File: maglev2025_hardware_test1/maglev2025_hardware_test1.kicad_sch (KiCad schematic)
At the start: 5 parts, among them U1 STM32G474RBTx, U2 ICM-42688-P, U3 LIS3MDLTR, U4 AT8236

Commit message: update
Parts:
- added C1: 10u, Capacitor_SMD:C_1206_3216Metric, symbol Device:C
- added C2: 100u 25V, Capacitor_THT:CP_Radial_D6.3mm_P2.50mm, symbol Device:C_Polarized
- added R1: 10m, Resistor_SMD:R_2512_6332Metric, symbol Device:R_US
- added R2: 100m, Resistor_SMD:R_2512_6332Metric, symbol Device:R
- added U5: INA240A1PW, Package_SO:TSSOP-8_4.4x3mm_P0.65mm, symbol Amplifier_Current:INA240A1PW
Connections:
- net at L1.1 (-): now also U4.6 (OUT1)
- net at L1.2 (+): now also R1.1, U5.2 (+)
- net GND: now reaches U4.1 (GND), U4.9 (GND)
- net GND: now also C1.2, C2.2, R2.1, U5.1 (GND), U5.4 (GND), U5.6 (REF2)
- net CTRL_A2: now reaches U4.2 (IN2)
- net CTRL_A1: now reaches U4.3 (IN1)
- net +3.3V: now reaches U4.4 (VREF)
- net +3.3V: now also U5.5 (V+), U5.7 (REF1)
- net VPP: now reaches U4.5 (VM)
- net VPP: now also C1.1, C2.1
- net at U4.7 (ISEN): now also R2.2
- net at U4.8 (OUT2): now also R1.2, U5.3 (-)
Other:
- moved on the sheet: L1, U2, U4

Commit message: schemetic and pin assignment
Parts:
- removed U2: ICM-42688-P, 0_RM2024:PQFN50P300X250X97-14N, symbol 0_RM2024:ICM-42688-P
- removed U3: LIS3MDLTR, 0_RM2024:XDCR_LIS3MDLTR, symbol 0_RM2024:LIS3MDLTR
- added C10, C9: 100u 16V, Capacitor_THT:CP_Radial_D6.3mm_P2.50mm, symbol Device:C_Polarized
- added C11: 10u, Capacitor_SMD:C_0603_1608Metric, symbol Device:C
- added C12, C13, C14, C15, C16, C17, C18, C19, C20, C23, C25, C27, C28, C31, C32, C33: 100n, Capacitor_SMD:C_0603_1608Metric, symbol Device:C
- added C21, C30, C40, C41: 100n, Capacitor_SMD:C_0603_1608Metric, symbol Device:C_Small
- added C22: 20p, Capacitor_SMD:C_0603_1608Metric, symbol Device:C_Small
- added C24, C26, C29: 10u, Capacitor_SMD:C_1206_3216Metric, symbol Device:C_Small
- added C3, C5, C6: 10u, Capacitor_SMD:C_1206_3216Metric, symbol Device:C
- added C36, C39, C78: 10u, Capacitor_SMD:C_0603_1608Metric, symbol Device:C_Small
- added C38: 10n, Capacitor_SMD:C_0603_1608Metric, symbol Device:C_Small
- added C4, C7, C8: 100u 25V, Capacitor_THT:CP_Radial_D6.3mm_P2.50mm, symbol Device:C_Polarized
- added D4: SMAJ12A, Diode_SMD:D_SMA, symbol Diode:SMAJ24A
- added D5: SMF5.0A, Diode_SMD:D_SMF, symbol Diode:SMAJ5.0A
- added F1: 1A, Fuse:Fuse_1206_3216Metric, symbol Device:Fuse
- added J20: PWRIn, Connector_AMASS:AMASS_XT30U-M_1x02_P5.0mm_Vertical, symbol Connector_Generic:Conn_01x02
- added J28: SWD, Connector_Molex:Molex_PicoBlade_53261-0471_1x04-1MP_P1.25mm_Horizontal, symbol Connector_Generic_MountingPin:Conn_01x04_MountingPin
- added L2, L3, L4: ElectromagneticActor, Inductor_SMD:L_APV_APH1030, symbol Device:ElectromagneticActor
- added L5: 6u8, Inductor_SMD:L_Sunlord_MWSA0402S, symbol Device:L
- added R10, R9: 10k, Resistor_SMD:R_0603_1608Metric, symbol Device:R
- added R11, R16: 33r, Resistor_SMD:R_0603_1608Metric, symbol Device:R
- added R12, R13, R14, R15: 33, Resistor_SMD:R_0603_1608Metric, symbol Device:R
- added R23: 53.6k, Resistor_SMD:R_0603_1608Metric, symbol Device:R_Small
- added R26: 10k, Resistor_SMD:R_0603_1608Metric, symbol Device:R_Small
- added R3, R5, R6: 100m, Resistor_SMD:R_2512_6332Metric, symbol Device:R
- added R4, R7, R8: 10m, Resistor_SMD:R_2512_6332Metric, symbol Device:R_US
- added RN1, RN2, RN3: 33x4, Resistor_SMD:R_Array_Convex_4x0603, symbol Device:R_Pack04
- added U10, U11, U7: INA240A1PW, Package_SO:TSSOP-8_4.4x3mm_P0.65mm, symbol Amplifier_Current:INA240A1PW
- added U12: RY8411, Package_TO_SOT_SMD:SOT-23-6, symbol RM24:SY8301
- added U13: RS3236, Package_TO_SOT_SMD:SOT-23-5, symbol Regulator_Linear:LDK130-12_SOT23_SOT353
- added U2: LIS3MDL, Package_LGA:LGA-12_2x2mm_P0.5mm, symbol Sensor_Magnetic:LIS3MDL
- added U6, U8, U9: AT8236, Package_SO:Texas_HTSOP-8-1EP_3.9x4.9mm_P1.27mm_EP2.95x4.9mm_Mask2.4x3.1mm_ThermalVias, symbol Driver_Motor:DRV8870DDA
- added Y1: 25MHz, Crystal:Crystal_SMD_3225-4Pin_3.2x2.5mm, symbol Device:Crystal_GND24
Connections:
- net +3.3V: now also U1.1 (VBAT), U1.16 (VDD), U1.29 (VDDA), U1.32 (VDD), U1.48 (VDD), U1.64 (VDD), C13.1, C14.1, C15.1, C16.1, C17.1, C18.1, C19.1, C32.1, C33.1, C39.1, C41.1, R9.1, U10.5 (V+), U10.7 (REF1), U11.5 (V+), U11.7 (REF1), U13.5 (OUT), U2.5 (Vdd), U2.6 (Vdd_IO), U6.4 (VREF), U7.5 (V+), U7.7 (REF1), U8.4 (VREF), U9.4 (VREF)
- net CTRL_A1: now also RN1.4 (R4.1)
- net CTRL_A2: now also RN1.3 (R3.1)
- net GND: now also U1.15 (VSS), U1.27 (VSSA), U1.31 (VSS), U1.47 (VSS), U1.63 (VSS), C10.2, C11.2, C12.2, C13.2, C14.2, C15.2, C16.2, C17.2, C18.2, C19.2, C20.1, C23.2, C24.2, C25.1, C26.2, C27.1, C28.1, C29.2, C3.2, C30.2, C31.1, C32.2, C33.2, C36.2, C38.2, C39.2, C4.2, C40.2, C41.2, C5.2, C6.2, C7.2, C78.2, C8.2, C9.2, D4.2 (A2), D5.2 (A2), J20.1 (Pin_1), J28.3 (Pin_3), J28.MP (MountPin), R10.2, R26.2, R3.1, R5.1, R6.1, U10.1 (GND), U10.4 (GND), U10.6 (REF2), U11.1 (GND), U11.4 (GND), U11.6 (REF2), U12.2 (GND), U13.2 (GND), U2.12 (GND), U2.2 (GND), U2.3 (GND), U6.1 (GND), U6.9 (GND), U7.1 (GND), U7.4 (GND), U7.6 (REF2), U8.1 (GND), U8.9 (GND), U9.1 (GND), U9.9 (GND), Y1.2, Y1.4
- net VPP: now also C10.1, C29.1, C3.1, C30.1, C4.1, C5.1, C6.1, C7.1, C8.1, D4.1 (A1), F1.2, U12.4 (EN), U12.5 (IN), U6.5 (VM), U8.5 (VM), U9.5 (VM)
- net ISENSE_A_MCU: now reaches U1.18 (PA4)
- net ISENSE_A_MCU: now also R12.1
- net ISENSE_B_MCU: now reaches U1.20 (PA6)
- net ISENSE_B_MCU: now also R13.1
- net ISENSE_C_MCU: now reaches U1.22 (PC4)
- net ISENSE_C_MCU: now also R14.1
- net ISENSE_D_MCU: now reaches U1.26 (PB2)
- net ISENSE_D_MCU: now also R15.1
- net VREF: now reaches U1.28 (VREF+)
- net VREF: now also C11.1, C12.1
- net MCU_C1: now reaches U1.34 (PB12)
- net MCU_C1: now also RN2.5 (R4.2)
- net MCU_C2: now reaches U1.35 (PB13)
- net MCU_C2: now also RN2.6 (R3.2)
- net MCU_D1: now reaches U1.36 (PB14)
- net MCU_D1: now also RN2.7 (R2.2)
- net MCU_D2: now reaches U1.37 (PB15)
- net MCU_D2: now also RN2.8 (R1.2)
- net MCU_A1: now reaches U1.42 (PA8)
- net MCU_A1: now also RN1.5 (R4.2)
- net MCU_A2: now reaches U1.43 (PA9)
- net MCU_A2: now also RN1.6 (R3.2)
- net MCU_B1: now reaches U1.44 (PA10)
- net MCU_B1: now also RN1.7 (R2.2)
- net MCU_B2: now reaches U1.45 (PA11)
- net MCU_B2: now also RN1.8 (R1.2)
- net at U1.5 (PF0): now also Y1.1
- net at U1.56 (PB3): now also RN3.5 (R4.2)
- net at U1.57 (PB4): now also RN3.6 (R3.2)
- net at U1.58 (PB5): now also RN3.7 (R2.2)
- net at U1.59 (PB6): now also RN3.8 (R1.2)
- net at U1.6 (PF1): now also Y1.3
- net at U1.60 (PB7): now also R11.1
- net BOOT0: now reaches U1.61 (PB8)
- net BOOT0: now also R10.1
- net at U1.62 (PB9): now also R16.1
- net NRST: now reaches U1.7 (PG10)
- net NRST: now also C20.2, R9.2
- net ISENSE_A: now reaches U5.8
- net ISENSE_A: now also C25.2, R12.2
- new net: L3.1 (-), U8.6 (OUT1)
- new net: L3.2 (+), R7.1, U10.2 (+)
- new net: C21.2, L5.1, U12.6 (LX)
- new net: F1.1, J20.2 (Pin_2)
- new net: C23.1, U2.4 (C1)
- new net: C22.2, R23.2, R26.1, U12.3 (FB)
- new net: L2.2 (+), R4.1, U7.2 (+)
- new net: R4.2, U6.8 (OUT2), U7.3 (-)
- new net: L4.2 (+), R8.1, U11.2 (+)
- new net: R8.2, U11.3 (-), U9.8 (OUT2)
- new net: R7.2, U10.3 (-), U8.8 (OUT2)
- new net: L4.1 (-), U9.6 (OUT1)
- new net: R6.2, U9.7 (ISEN)
- new net: C38.1, U13.4 (BP)
- new net: C21.1, U12.1 (BS)
- new net: R3.2, U6.7 (ISEN)
- new net: R5.2, U8.7 (ISEN)
- new net: L2.1 (-), U6.6 (OUT1)
- new net 3V3_SWD: C78.1, J28.4 (Pin_4)
- new net 5V: C22.1, C24.1, C26.1, C36.1, C40.1, C9.1, D5.1 (A1), L5.2, R23.1, U13.1 (IN), U13.3 (EN)
- new net CTRL_B1: RN1.2 (R2.1), U6.3 (IN1)
- new net CTRL_B2: RN1.1 (R1.1), U6.2 (IN2)
- new net CTRL_C1: RN2.4 (R4.1), U8.3 (IN1)
- new net CTRL_C2: RN2.3 (R3.1), U8.2 (IN2)
- new net CTRL_D1: RN2.2 (R2.1), U9.3 (IN1)
- new net CTRL_D2: RN2.1 (R1.1), U9.2 (IN2)
- new net ISENSE_B: C27.2, R13.2, U7.8
- new net ISENSE_C: C28.2, R14.2, U10.8
- new net ISENSE_D: C31.2, R15.2, U11.8
- new net LIS3_CS: R11.2, U2.10 (~{CS})
- new net LIS3_DRY: RN3.1 (R1.1), U2.8 (DRDY)
- new net LIS3_INT: R16.2, U2.7 (INT)
- new net SPI1_MISO: RN3.3 (R3.1), U2.9 (SDO/SA1)
- new net SPI1_MOSI: RN3.2 (R2.1), U2.11 (SDA/SDI/SDO)
- new net SPI1_SCK: RN3.4 (R4.1), U2.1 (SCL/SPC)
- new net SWCLK: J28.2 (Pin_2)
- new net SWDIO: J28.1 (Pin_1)
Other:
- note added: "12V IN"
- note added: "SWD"
- moved on the sheet: C1, C2, L1, R1, R2, U1, U4, U5

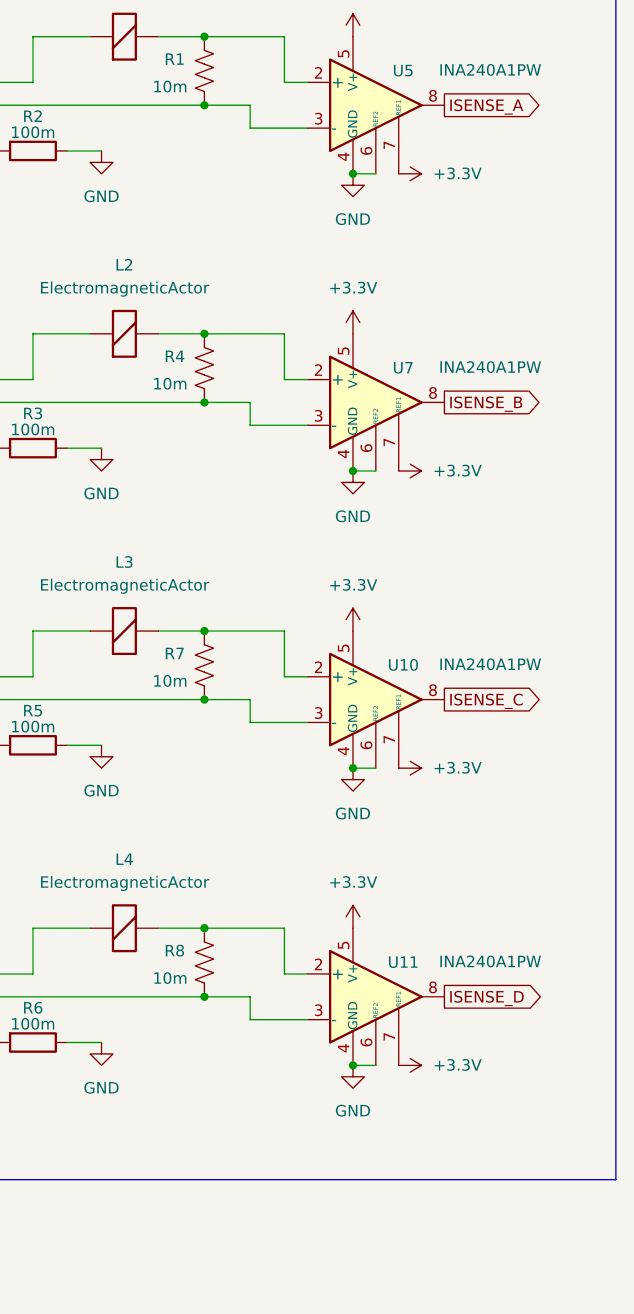
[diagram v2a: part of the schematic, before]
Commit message: Update schematic and ioc
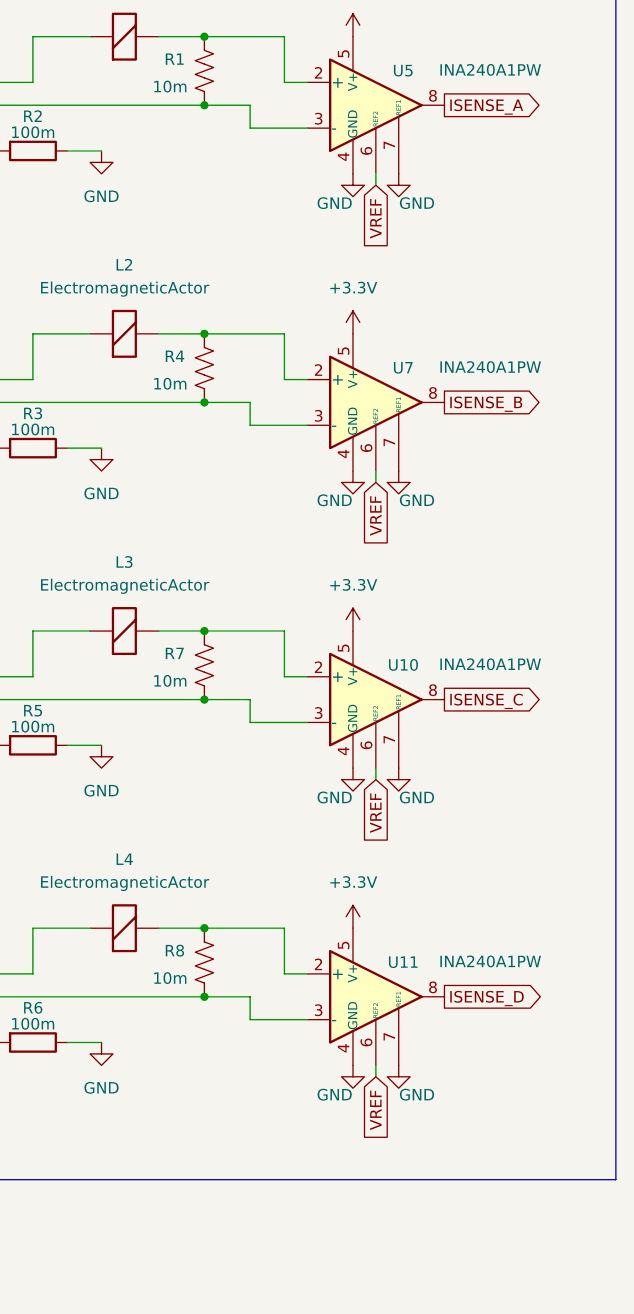
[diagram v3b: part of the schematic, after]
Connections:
- net +3.3V: no longer U10.7 (REF1), U11.7 (REF1), U5.7 (REF1), U7.7 (REF1)
- net GND: now also U10.7 (REF1), U11.7 (REF1), U5.7 (REF1), U7.7 (REF1); no longer U10.6 (REF2), U11.6 (REF2), U5.6 (REF2), U7.6 (REF2)
- net VREF: now also U10.6 (REF2), U11.6 (REF2), U5.6 (REF2), U7.6 (REF2)

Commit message: Layout mostly done
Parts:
- removed C23, C32, C33: 100n, Capacitor_SMD:C_0603_1608Metric, symbol Device:C
- removed C78: 10u, Capacitor_SMD:C_0603_1608Metric, symbol Device:C_Small
- removed C9: 100u 16V, Capacitor_THT:CP_Radial_D6.3mm_P2.50mm, symbol Device:C_Polarized
- removed U2: LIS3MDL, Package_LGA:LGA-12_2x2mm_P0.5mm, symbol Sensor_Magnetic:LIS3MDL
- added C13, C15, C39, C40, C41, C42, C43, C44, C45, C46, C47, C48, C49, C50: 100n, Capacitor_SMD:C_0603_1608Metric, symbol Device:C
- added C24: 100u, Capacitor_SMD:C_2220_5750Metric, symbol Device:C_Small
- added C51, C52: 20p, Capacitor_SMD:C_0603_1608Metric, symbol Device:C
- added C53: 10u, Capacitor_SMD:C_0603_1608Metric, symbol Device:C
- added D3: K34, Diode_SMD:D_SOD-123F, symbol Device:D_Schottky
- added F2: 0.5A, Fuse:Fuse_1206_3216Metric, symbol Device:Fuse
- added R19, R20: 33r, Resistor_SMD:R_0603_1608Metric, symbol Device:R
- added U2: TMAG5170-Q1, Package_SO:VSSOP-8_3x3mm_P0.65mm, symbol Sensor_Magnetic:TMAG5170-Q1
- C11: renamed from C16; value 100n -> 10u
- F1: value 1A -> 5A
- L2: renamed from L1; footprint Inductor_SMD:L_APV_APH1030 -> Connector_JST:JST_PH_B2B-PH-K_1x02_P2.00mm_Vertical
- L3: renamed from L2; footprint Inductor_SMD:L_APV_APH1030 -> Connector_JST:JST_PH_B2B-PH-K_1x02_P2.00mm_Vertical
- L4: renamed from L3; footprint Inductor_SMD:L_APV_APH1030 -> Connector_JST:JST_PH_B2B-PH-K_1x02_P2.00mm_Vertical
- L5: renamed from L4; footprint Inductor_SMD:L_APV_APH1030 -> Connector_JST:JST_PH_B2B-PH-K_1x02_P2.00mm_Vertical
- renumbered C11 to C1, C30 to C10, C17 to C12, C18 to C14, C21 to C16, C36 to C17, C40 to C18, C12 to C2, C22 to C20, C24 to C21, C26 to C22, C38 to C23, C39 to C25, C41 to C26, C1 to C27, C3 to C28, C5 to C29, C6 to C30, C2 to C31, C4 to C32, C7 to C33, C8 to C34, C25 to C35, C27 to C36, C28 to C37, C31 to C38, C13 to C4, C10 to C5, C14 to C6, C29 to C7, C15 to C8, C20 to C9, D4 to D1, D5 to D2, J28 to J1, J20 to J2, L5 to L1, R9 to R1, R15 to R10, R2 to R11, R3 to R12, R5 to R13, R6 to R14, R1 to R15, R4 to R16, R7 to R17, R8 to R18, R23 to R2, R26 to R3, R11 to R4, R10 to R5, R16 to R6, R12 to R7, R13 to R8, R14 to R9, RN3 to RN2, RN2 to RN3, U12 to U1, U7 to U10, U10 to U11, U11 to U12, U1 to U3, U13 to U4, U4 to U5, U8 to U7, U9 to U8, U5 to U9
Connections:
- net +3.3V: now also C13.1, C15.1, C43.1, C44.1, C45.1, C46.1, C53.1, F2.2, U2.5 (VCC)
- net 5V: now also D3.1 (K); no longer C21.1, C22.1, D2.1 (A1), L1.2
- net CTRL_A1: now also RN1.5 (R4.2); no longer RN1.4 (R4.1)
- net CTRL_A2: now also RN1.6 (R3.2); no longer RN1.3 (R3.1)
- net CTRL_B1: now also RN1.7 (R2.2); no longer RN1.2 (R2.1)
- net CTRL_B2: now also RN1.8 (R1.2); no longer RN1.1 (R1.1)
- net CTRL_C1: now also RN3.5 (R4.2); no longer RN3.4 (R4.1)
- net CTRL_C2: now also RN3.6 (R3.2); no longer RN3.3 (R3.1)
- net CTRL_D1: now also RN3.7 (R2.2); no longer RN3.2 (R2.1)
- net CTRL_D2: now also RN3.8 (R1.2); no longer RN3.1 (R1.1)
- net GND: now also C13.2, C15.2, C24.2, C39.2, C40.2, C41.2, C42.2, C43.2, C44.2, C45.2, C46.2, C47.2, C48.2, C49.2, C50.2, C51.2, C52.2, C53.2, U2.6 (GND), U2.7 (TEST)
- net LIS3_DRY: now also RN2.8 (R1.2); no longer RN2.1 (R1.1)
- net MCU_A1: now also RN1.4 (R4.1); no longer RN1.5 (R4.2)
- net MCU_A2: now also RN1.3 (R3.1); no longer RN1.6 (R3.2)
- net MCU_B1: now also RN1.2 (R2.1); no longer RN1.7 (R2.2)
- net MCU_B2: now also RN1.1 (R1.1); no longer RN1.8 (R1.2)
- net MCU_C1: now also RN3.4 (R4.1); no longer RN3.5 (R4.2)
- net MCU_C2: now also RN3.3 (R3.1); no longer RN3.6 (R3.2)
- net MCU_D1: now also RN3.2 (R2.1); no longer RN3.7 (R2.2)
- net MCU_D2: now also RN3.1 (R1.1); no longer RN3.8 (R1.2)
- net SPI1_MISO: now also RN2.6 (R3.2), U2.3 (MISO); no longer RN2.3 (R3.1)
- net SPI1_MOSI: now also RN2.7 (R2.2), U2.2 (MOSI); no longer RN2.2 (R2.1)
- net SPI1_SCK: now also RN2.5 (R4.2), U2.1 (SCLK); no longer RN2.4 (R4.1)
- net SWCLK: now also R19.2
- net SWDIO: now also R20.2
- net VPP: now also C39.1, C40.1, C41.1, C42.1
- net VREF: now also C47.1, C48.1, C49.1, C50.1
- net at U3.5 (PF0), Y1.1: now also C52.1
- net at U3.50 (PA14): now also R19.1
- net at U3.51 (PA15): now also R20.1
- net at U3.56 (PB3): now also RN2.4 (R4.1); no longer RN2.5 (R4.2)
- net at U3.57 (PB4): now also RN2.3 (R3.1); no longer RN2.6 (R3.2)
- net at U3.58 (PB5): now also RN2.2 (R2.1); no longer RN2.7 (R2.2)
- net at U3.59 (PB6): now also RN2.1 (R1.1); no longer RN2.8 (R1.2)
- net at U3.6 (PF1), Y1.3: now also C51.1
- net 3V3_SWD: no longer names the net of J1.4 (Pin_4)
- net 3V3_SWD: now also F2.1
- new net: C21.1, C22.1, C24.1, D2.1 (A1), D3.2 (A), L1.2
- new net ~{MAG_ALRT}: U2.8 (~{ALERT})
- new net ~{MAG_CS}: U2.4 (~{CS})
- no-connect marks 0 -> 28
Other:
- moved on the sheet: C20, D2, R2, R3, RN1, RN2, RN3

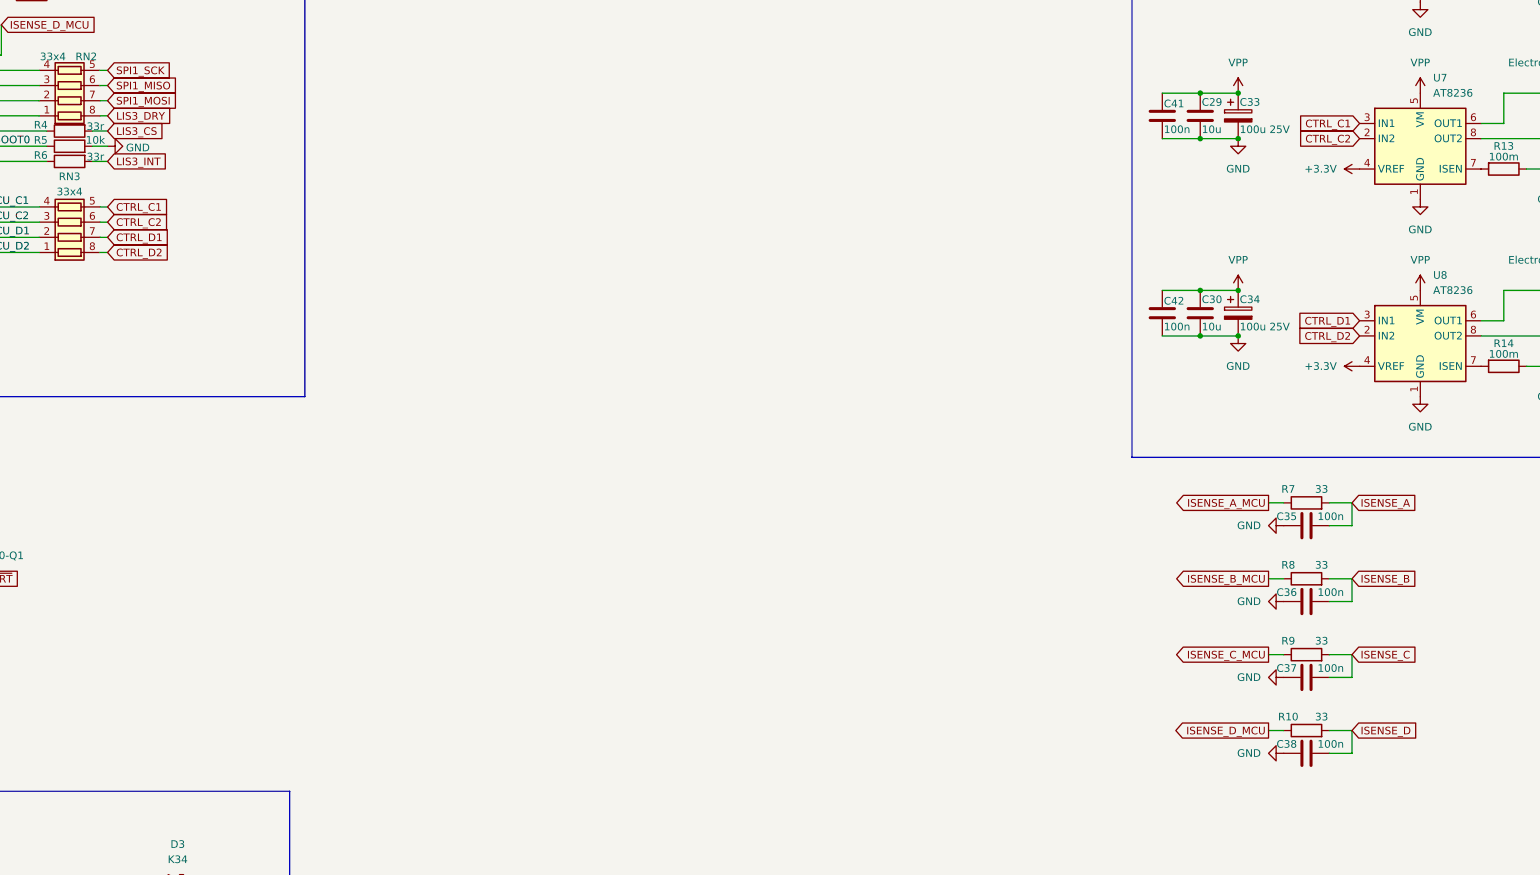
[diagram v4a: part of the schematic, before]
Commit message: Layout routing done, checking test
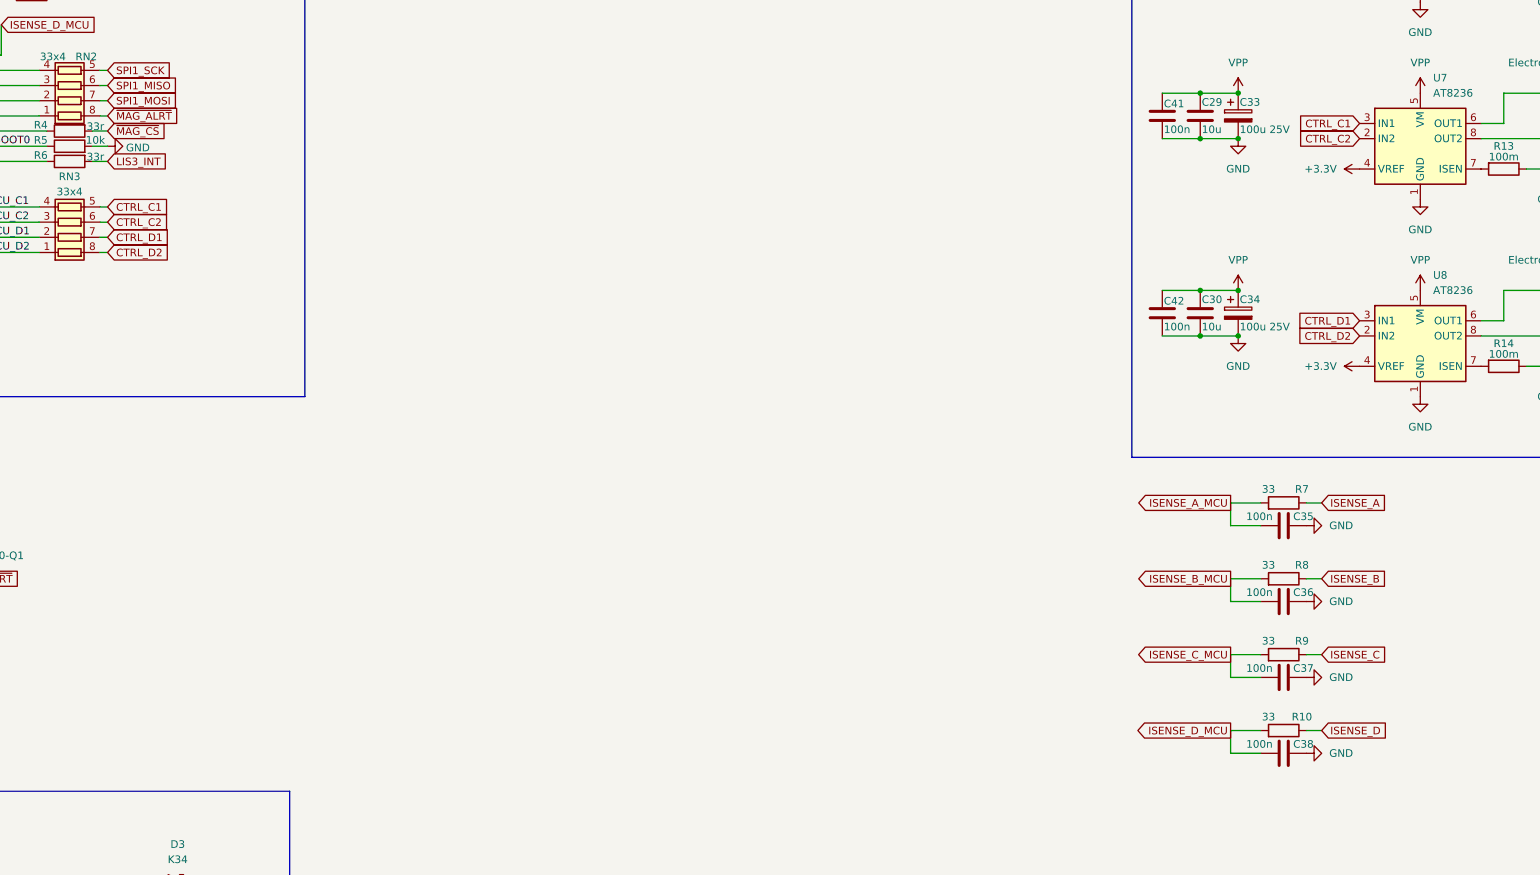
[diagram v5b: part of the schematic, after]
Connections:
- net LIS3_CS is gone; now on net ~{MAG_CS}: R4.2
- net LIS3_DRY is gone; now on net ~{MAG_ALRT}: RN2.8 (R1.2)
- net ISENSE_A: now also R7.1; no longer C35.2, R7.2
- net ISENSE_A_MCU: now also C35.2, R7.2; no longer R7.1
- net ISENSE_B: now also R8.1; no longer C36.2, R8.2
- net ISENSE_B_MCU: now also C36.2, R8.2; no longer R8.1
- net ISENSE_C: now also R9.1; no longer C37.2, R9.2
- net ISENSE_C_MCU: now also C37.2, R9.2; no longer R9.1
- net ISENSE_D: now also R10.1; no longer C38.2, R10.2
- net ISENSE_D_MCU: now also C38.2, R10.2; no longer R10.1
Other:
- moved on the sheet: C35, C36, C37, C38, R10, R7, R8, R9

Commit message: Almost Complete
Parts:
- added H1, H2, H3, H4, H5, H6: MountingHole_Pad, MountingHole:MountingHole_3.2mm_M3_DIN965_Pad_TopBottom, symbol Mechanical:MountingHole_Pad
